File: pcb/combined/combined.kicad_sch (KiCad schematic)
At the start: 34 parts, among them J1 CTRL, J2 MAINS_IN, J3 VALVE, J4 PUMP, Q1 SS8050, Q2 BT136S, Q3 SS8050, Q4 BT136S, U1 MOC3043M, U2 MOC3023M, U3 EL817C

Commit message: Combine the AC control and sensors circuits on the combined board
The renamed accontrol project now carries the sensors controller on two
new sheets: XIAO, CAN, I2C pull-ups with TMP102 and ADS1115, FLOW, boiler
output, status LED and the 5 V, CAN, BOILER, PRESSURE and FLOW headers.
The 5-pin control header, the Grove I2C headers and the VALVE header are
dropped: DIM, ZC and SSR run as tracks to XIAO D0, D2 and D10. Sensors
parts that clashed with AC references are renumbered, the BOM and design
notes follow, and +5V/+3V3 get the 0.3 mm POWER net class from sensors.

Co-Authored-By: Claude Opus 5.5 <noreply@anthropic.com>
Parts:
- removed J1: CTRL, Connector_JST:JST_XH_B5B-XH-A_1x05_P2.50mm_Vertical, symbol Connector_Generic:Conn_01x05
- F1: footprint Accontrol_Local:F2410 -> Combined_Local:F2410
- J2, J3, J4: footprint Accontrol_Local:CONN-TH_P3.96_HT396R-3.96-2P -> Combined_Local:CONN-TH_P3.96_HT396R-3.96-2P
- U1, U2: footprint Accontrol_Local:SMDIP-6_W9.53mm_Slot -> Combined_Local:SMDIP-6_W9.53mm_Slot
- U3: footprint Accontrol_Local:SMDIP-4_W9.53mm_Slot -> Combined_Local:SMDIP-4_W9.53mm_Slot
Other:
- added sheet Controller (combined_controller.kicad_sch)
- added sheet Interfaces (combined_interfaces.kicad_sch)
- note added: "1 / Logic inputs DIM, ZC, SSR and 3V3 from the XIAO (Controller sheet)"
- note added: "CoffeeFlow - combined board, AC side (pump dimmer + valve SSR)"
- note removed: "1 / DC connector"
- note removed: "CoffeeFlow - AC control board (pump dimmer + valve SSR)"
- title: AC control - pump dimmer and valve SSR -> Combined - AC side: pump dimmer, valve SSR, zero-cross

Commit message: Route the combined board to a clean DRC and export it for JLCPCB
Rules follow IEC 60335-1 for functional insulation: 2.2 mm between mains
nets, 1.5 mm or 1.1 mm between mains nets a few volts apart, and the
track-into-pad exception tied to the part a track enters. The HT3.96
connectors get oval pads, the datasheet's 1.6 mm holes and a milled slot
between L and N. C2/C3 move to 1812, R12 splits into R12 + R27, and every
part has its JLCPCB number. The exporter accepts polygon outlines, and the
placement corrections come from the supplier footprints. H2 and H3 are
added to the schematic.

Co-Authored-By: Claude Opus 5.5 <noreply@anthropic.com>
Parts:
- removed C1: 1uF, Capacitor_SMD:C_0603_1608Metric, symbol Device:C
- added R27: 510, Resistor_SMD:R_1206_3216Metric, symbol Device:R
- C2, C3: footprint Capacitor_SMD:C_1206_3216Metric -> Capacitor_SMD:C_1812_4532Metric; LCSC (none) -> C394164; MPN (none) -> FV43X103K102EFG
- D1, D2: LCSC (none) -> C2286; MPN (none) -> KT-0603R
- Q1, Q3: LCSC (none) -> C2150
- R1, R11, R4, R8: LCSC (none) -> C21190; MPN (none) -> 0603WAF1001T5E
- R10, R3: LCSC (none) -> C22828; MPN (none) -> 0603WAF1800T5E
- R12: value 1k -> 510; LCSC (none) -> C17991; MPN (none) -> 1206W4F5100T5E; Note MT2 series resistor, gate driven directly (RobotDyn design) -> MT2 series resistor with R27, 2 x 510R: each 1206 sees at m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
- R16: LCSC (none) -> C25804; MPN (none) -> 0603WAF1002T5E
- R2, R9: LCSC (none) -> C23162; MPN (none) -> 0603WAF4701T5E
- R5: LCSC (none) -> C17932; MPN (none) -> 1206W4F3600T5E
- R6: LCSC (none) -> C17930; MPN (none) -> 1206W4F3300T5E
- R7: LCSC (none) -> C22198; MPN (none) -> 1206W4F390JT5E
- U1: LCSC (none) -> C41809; MPN MOC3043M -> MOC3043SR2M
- U2: LCSC (none) -> C40701; MPN MOC3023M -> MOC3023SR2M
- U3: LCSC (none) -> C2912100
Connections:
- net L: now also R27.1; no longer R12.2
- new net: R12.2, R27.2

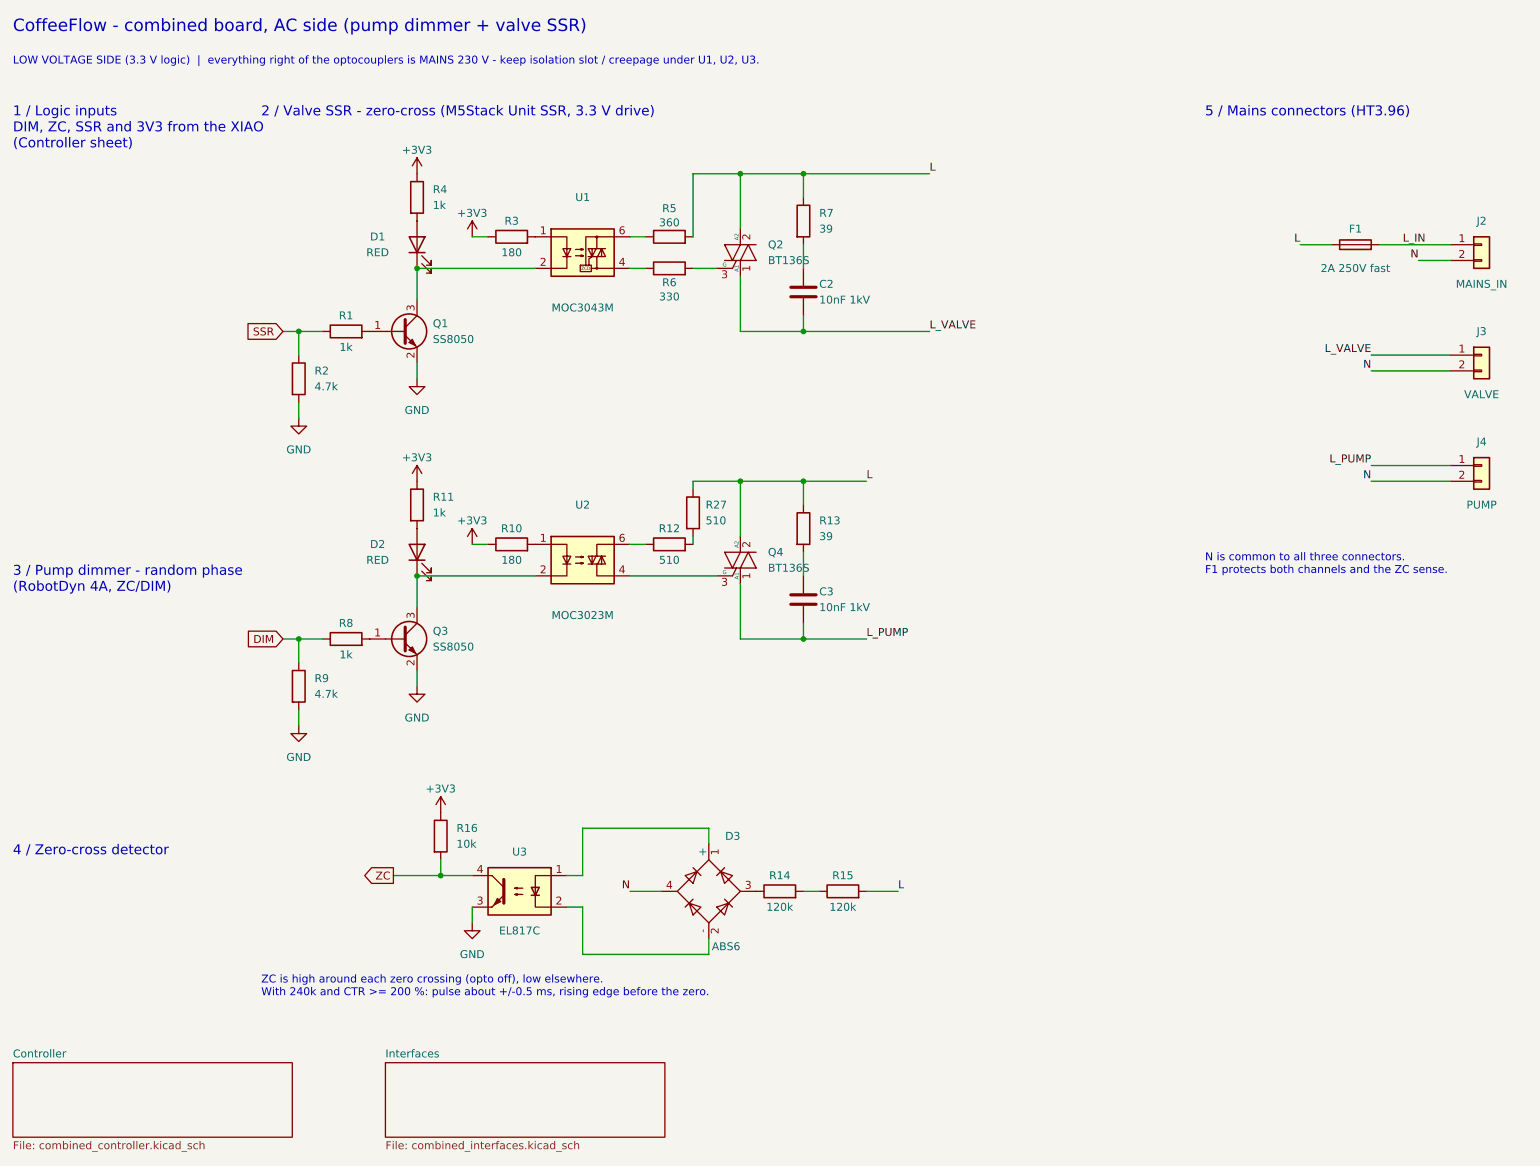
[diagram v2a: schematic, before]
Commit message: Draw the combined v2 schematic: 24 V buck and isolated gear pump interface
The pump dimmer and the zero-cross detector leave the board; the 230 V
valve channel stays. J7 brings 24 V from the pump supply to an
LMR33630A buck (5.02 V, enable at 18.4 V, off at 16.9 V), and J1 now sends
5 V to the screen. Two EL817C keep the pump's signal wires on their
isolated side: U8 turns the 1 kHz PWM on GPIO1 into a filtered setpoint
from the pump's own 5 V, U9 brings the tachometer back to GPIO3. DIM and
ZC become PUMP_SPEED and PUMP_TACHO.

The XIAO 5V pin is its USB VBUS with no diode; no diode is added either,
so USB is never plugged in with the XIAO on the board. New parts take new
references, so that no low-voltage net inherits a stale Mains netclass
pattern; those patterns and the pump and zero-cross DRC rules are gone.

F1 drops to 0.5 A, now that it protects the valve alone, and the AC
tracks to 1 mm. J3 is reversed so that its N faces N on J2. The HT396R
outline follows the Kefa drawing, and J8 becomes an HT396V header whose
screw plug takes the 0.75 mm² wires to the boiler SSR.

The board has been updated from the schematic; placement and routing are
still in progress.

Co-Authored-By: Claude Opus 5.5 <noreply@anthropic.com>
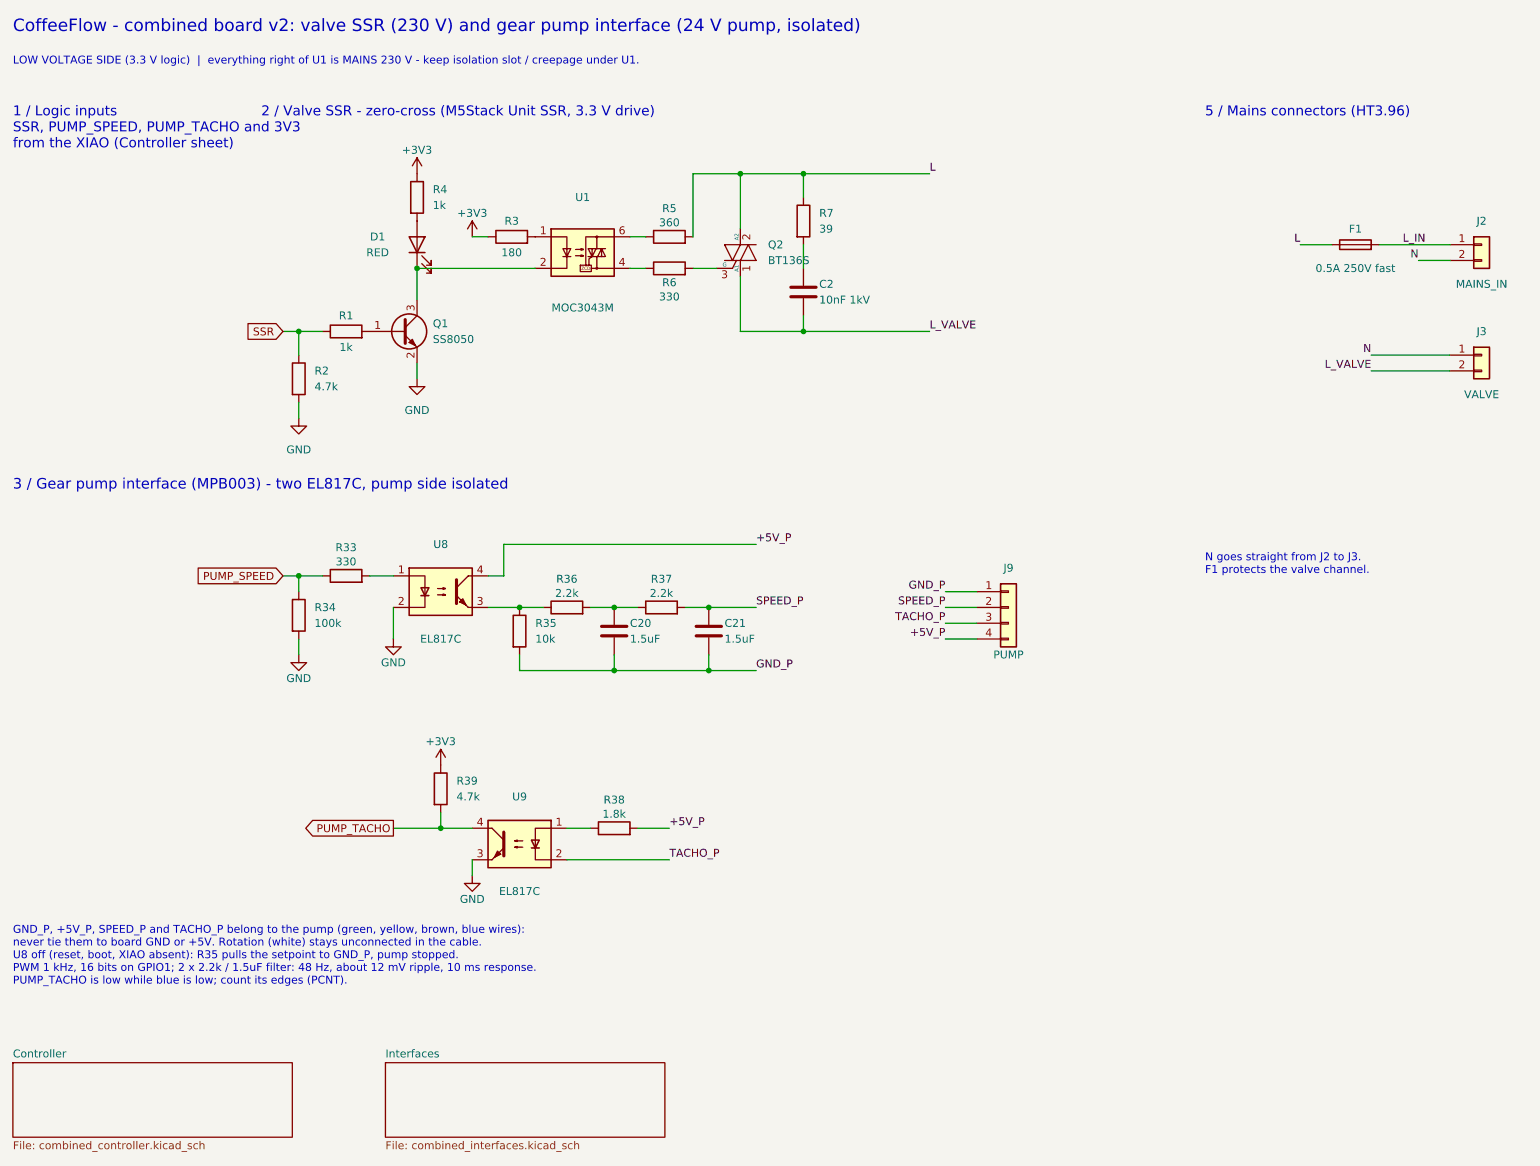
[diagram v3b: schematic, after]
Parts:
- removed C3: 10nF 1kV, Capacitor_SMD:C_1812_4532Metric, symbol Device:C
- removed D2: RED, LED_SMD:LED_0603_1608Metric, symbol Device:LED
- removed D3: ABS6, Diode_SMD:Diode_Bridge_Diotec_ABS, symbol Diode_Bridge:ABS6
- removed J4: PUMP, Combined_Local:CONN-TH_P3.96_HT396R-3.96-2P, symbol Connector_Generic:Conn_01x02
- removed Q3: SS8050, Package_TO_SOT_SMD:SOT-23, symbol Transistor_BJT:Q_NPN_BEC
- removed Q4: BT136S, Package_TO_SOT_SMD:TO-252-2, symbol Triac_Thyristor:BT136-600
- removed R10: 180, Resistor_SMD:R_0603_1608Metric, symbol Device:R
- removed R11, R8: 1k, Resistor_SMD:R_0603_1608Metric, symbol Device:R
- removed R12, R27: 510, Resistor_SMD:R_1206_3216Metric, symbol Device:R
- removed R13: 39, Resistor_SMD:R_1210_3225Metric, symbol Device:R
- removed R14, R15: 120k, Resistor_SMD:R_1210_3225Metric, symbol Device:R
- removed R16: 10k, Resistor_SMD:R_0603_1608Metric, symbol Device:R
- removed R9: 4.7k, Resistor_SMD:R_0603_1608Metric, symbol Device:R
- removed U2: MOC3023M, Combined_Local:SMDIP-6_W9.53mm_Slot, symbol Relay_SolidState:MOC3023M
- removed U3: EL817C, Combined_Local:SMDIP-4_W9.53mm_Slot, symbol Isolator:EL817
- added C20, C21: 1.5uF, Capacitor_SMD:C_0805_2012Metric, symbol Device:C
- added J9: PUMP, Connector_JST:JST_XH_B4B-XH-A_1x04_P2.50mm_Vertical, symbol Connector_Generic:Conn_01x04
- added R33: 330, Resistor_SMD:R_0603_1608Metric, symbol Device:R
- added R34: 100k, Resistor_SMD:R_0603_1608Metric, symbol Device:R
- added R35: 10k, Resistor_SMD:R_0603_1608Metric, symbol Device:R
- added R36, R37: 2.2k, Resistor_SMD:R_0603_1608Metric, symbol Device:R
- added R38: 1.8k, Resistor_SMD:R_0603_1608Metric, symbol Device:R
- added R39: 4.7k, Resistor_SMD:R_0603_1608Metric, symbol Device:R
- added U8, U9: EL817C, Package_DIP:SMDIP-4_W9.53mm, symbol Isolator:EL817
- F1: value 2A 250V fast -> 0.5A 250V fast; LCSC C83797 -> C91409; MPN MF2410F2.000TM -> MF2410F0.500TM
- J3: Note 1 L (switched), 2 N -> 1 N, 2 L (switched): N next to N of J2
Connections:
- net +3V3: now also R39.1
- net GND: now also R34.2, U8.2, U9.3
- net L_VALVE: now also J3.2 (Pin_2); no longer J3.1 (Pin_1)
- net N: now also J3.1 (Pin_1); no longer J3.2 (Pin_2)
- new net: C20.1, R36.2, R37.1
- new net: R38.1, U9.1
- new net: R33.2, U8.1
- new net: R35.1, R36.1, U8.3
- new net +5V_P: J9.4 (Pin_4), R38.2, U8.4
- new net GND_P: C20.2, C21.2, J9.1 (Pin_1), R35.2
- new net PUMP_SPEED: R33.1, R34.1
- new net PUMP_TACHO: R39.2, U9.4
- new net SPEED_P: C21.1, J9.2 (Pin_2), R37.2
- new net TACHO_P: J9.3 (Pin_3), U9.2
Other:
- note added: "1 / Logic inputs SSR, PUMP_SPEED, PUMP_TACHO and 3V3 from the XIAO (Controller sheet)"
- note added: "3 / Gear pump interface (MPB003) - two EL817C, pump side isolated"
- note added: "CoffeeFlow - combined board v2: valve SSR (230 V) and gear pump interface (24 V pump, isolated)"
- note added: "GND_P, +5V_P, SPEED_P and TACHO_P belong to the pump (green, yellow, brown, blue wires): never tie them to board GND or +5V. Rotation (white) stays unconnected in the cable. U8 off (reset, boot, XIAO absent): R35 pulls the setpoint to GND_P, pump stopped. PWM 1 kHz, 16 bits on GPIO1; 2 x 2.2k / 1.5uF filter: 48 Hz, about 12 mV ripple, 10 ms response. PUMP_TACHO is low while blue is low; count its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"
- note added: "LOW VOLTAGE SIDE (3.3 V logic) | everything right of U1 is MAINS 230 V - keep isolation slot / creepage under U1."
- note added: "N goes straight from J2 to J3. F1 protects the valve channel."
- note removed: "1 / Logic inputs DIM, ZC, SSR and 3V3 from the XIAO (Controller sheet)"
- note removed: "3 / Pump dimmer - random phase (RobotDyn 4A, ZC/DIM)"
- note removed: "4 / Zero-cross detector"
- note removed: "CoffeeFlow - combined board, AC side (pump dimmer + valve SSR)"
- note removed: "LOW VOLTAGE SIDE (3.3 V logic) | everything right of the optocouplers is MAINS 230 V - keep isolation slot / creepage under U1, U2, U3."
- note removed: "N is common to all three connectors. F1 protects both channels and the ZC sense."
- note removed: "ZC is high around each zero crossing (opto off), low elsewhere. With 240k and CTR >= 200 %: pulse about +/-0.5 ms, rising edge before the zero."
- title: Combined - AC side: pump dimmer, valve SSR, zero-cross -> Combined - valve SSR (230 V) and gear pump interface

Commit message: Route combined v2: buck layout, POWER class with GND, GPIO table on the back
Shrink F.Fab texts to 0.5 mm and silkscreen texts to 0.8 mm. Put GND in
the POWER net class and enforce its 0.3 mm minimum by a DRC rule, with a
0.2 mm neck-down allowed at the TMP102. Add the XIAO GPIO table on
B.SilkS and the 24 V and 230 V ratings.

Swap R5 to C163378 and U6 to ADS1115IDGST (C468683), same parts in stock.
Fix the JLCPCB placement of U5 (+270) and J9 (pin-row midpoint, +180).

Co-Authored-By: Claude Opus 5.5 <noreply@anthropic.com>
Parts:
- R5: LCSC C17932 -> C163378; MPN 1206W4F3600T5E -> RC1206FR-07360RL
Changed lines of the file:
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@@
 			)
 		)
-		(property "MPN" "1206W4F3600T5E"
+		(property "MPN" "RC1206FR-07360RL"
 			(at 125.73 46.99 90)
 			(hide yes)
@@
 			)
 		)
-		(property "LCSC" "C17932"
+		(property "LCSC" "C163378"
 			(at 125.73 46.99 90)
 			(hide yes)
